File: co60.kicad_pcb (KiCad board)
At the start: 2 copper layers, 285 x 95.1 mm, 251 parts, among them J1 Conn_01x06, Q1 FMMT493TA, SW1 SW_Push, U1 ATMEGA32U4, Y1 16MHz

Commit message: Update: Clean up routing and add some header labels
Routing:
- net LEDPWM: track 25.7 -> 22.6 mm
- net ROW2: track 324.2 -> 322.6 mm
- net LEDGND: track 1543.0 -> 1541.9 mm
- net ROW1: track 329.4 -> 328.6 mm
- net COL11: track 292.1 -> 291.4 mm
- net COL10: track 262.8 -> 262.1 mm
- net COL13: track 348.2 -> 348.9 mm
- net COL3: track 107.2 -> 107.9 mm
- net COL12: track 292.9 -> 293.6 mm
- net Net-(K_LGUI1-Pad4): track 12.3 -> 11.7 mm
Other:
- board text added: "GND"
- board text added: "MISO"
- board text added: "MOSI"
- board text added: "RST"
- board text added: "SCLK"
- board text added: "VCC"

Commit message: Update: A couple of routes
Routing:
- net Net-(D25-Pad2): track 6.72 -> 7.26 mm
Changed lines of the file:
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@@
     (thickness 1.6)
     (drawings 6)
-    (tracks 2795)
+    (tracks 2799)
     (zones 0)
     (modules 251)
@@
   (segment (start 256.83025 75.8825) (end 258.365625 77.417875) (width 0.254) (layer B.Cu) (net 31))
   (segment (start 258.365625 77.417875) (end 258.365625 78.121875) (width 0.254) (layer B.Cu) (net 31))
-  (segment (start 271.62125 75.8825) (end 273.860625 78.121875) (width 0.254) (layer B.Cu) (net 32))
-  (segment (start 273.860625 78.121875) (end 277.415625 78.121875) (width 0.254) (layer B.Cu) (net 32))
-  (segment (start 290.67125 75.8825) (end 292.910625 78.121875) (width 0.254) (layer B.Cu) (net 33))
-  (segment (start 292.910625 78.121875) (end 296.465625 78.121875) (width 0.254) (layer B.Cu) (net 33))
+  (segment (start 271.62125 75.8825) (end 275.88025 75.8825) (width 0.254) (layer B.Cu) (net 32))
+  (segment (start 275.88025 75.8825) (end 277.415625 77.417875) (width 0.254) (layer B.Cu) (net 32))
+  (segment (start 277.415625 77.417875) (end 277.415625 78.121875) (width 0.254) (layer B.Cu) (net 32))
+  (segment (start 271.62125 75.8825) (end 271.71015 75.9714) (width 0.254) (layer B.Cu) (net 32))
+  (segment (start 290.67125 75.8825) (end 294.93025 75.8825) (width 0.254) (layer B.Cu) (net 33))
+  (segment (start 294.93025 75.8825) (end 296.465625 77.417875) (width 0.254) (layer B.Cu) (net 33))
+  (segment (start 296.465625 77.417875) (end 296.465625 78.121875) (width 0.254) (layer B.Cu) (net 33))
+  (segment (start 290.67125 75.8825) (end 290.70935 75.9206) (width 0.254) (layer B.Cu) (net 33))
   (segment (start 309.72125 75.8825) (end 313.98025 75.8825) (width 0.254) (layer B.Cu) (net 34))
   (segment (start 313.98025 75.8825) (end 315.515625 77.417875) (width 0.254) (layer B.Cu) (net 34))

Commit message: Update: Temporarily increase my net clearance values, and re-routing
I noticed in some other designs that the traces were farther
from drill holes and pads than I was putting mine, so I
figured I'd change that. I'm temporarily increasing
my clearance to 0.35 (from 0.2032) and I'm using the
OpenGL router to move my traces farther from holes and
pads. I'll put my clearance back when I'm done. The next switch
to adjust is K_#8
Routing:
- net ROW0: track 365.3 -> 366.2 mm
- net Net-(K_#7-Pad4): track 4.16 -> 5.07 mm
- net Net-(K_#6-Pad4): track 4.28 -> 5.07 mm
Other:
- net class Default: clearance 0.2032 -> 0.35
- net class Power: clearance 0.2032 -> 0.35
- rule trace_clearance: 0.2032 -> 0.35

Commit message: Update: More routing adjustments to increase clearances
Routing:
- net VCC: track 1753.0 -> 1755.1 mm
- net ROW0: track 366.2 -> 364.7 mm, vias 6 -> 8
- net ROW1: track 328.6 -> 329.1 mm, vias 6 -> 8

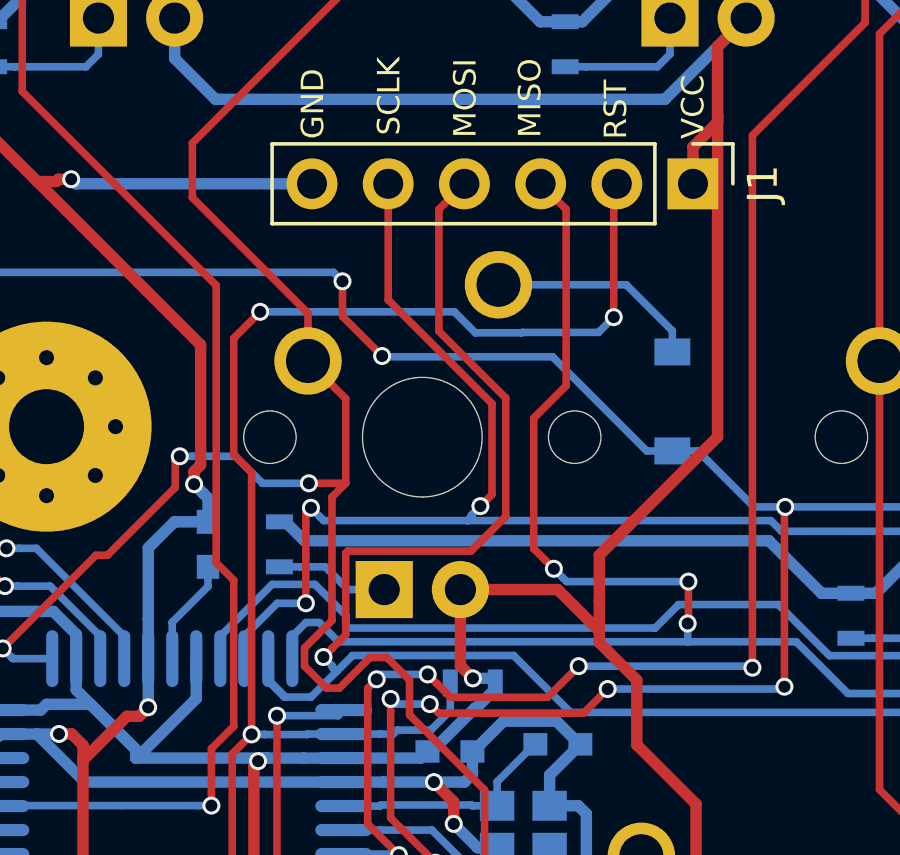
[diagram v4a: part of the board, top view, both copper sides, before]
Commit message: Update: Move more tracks to increase clearance
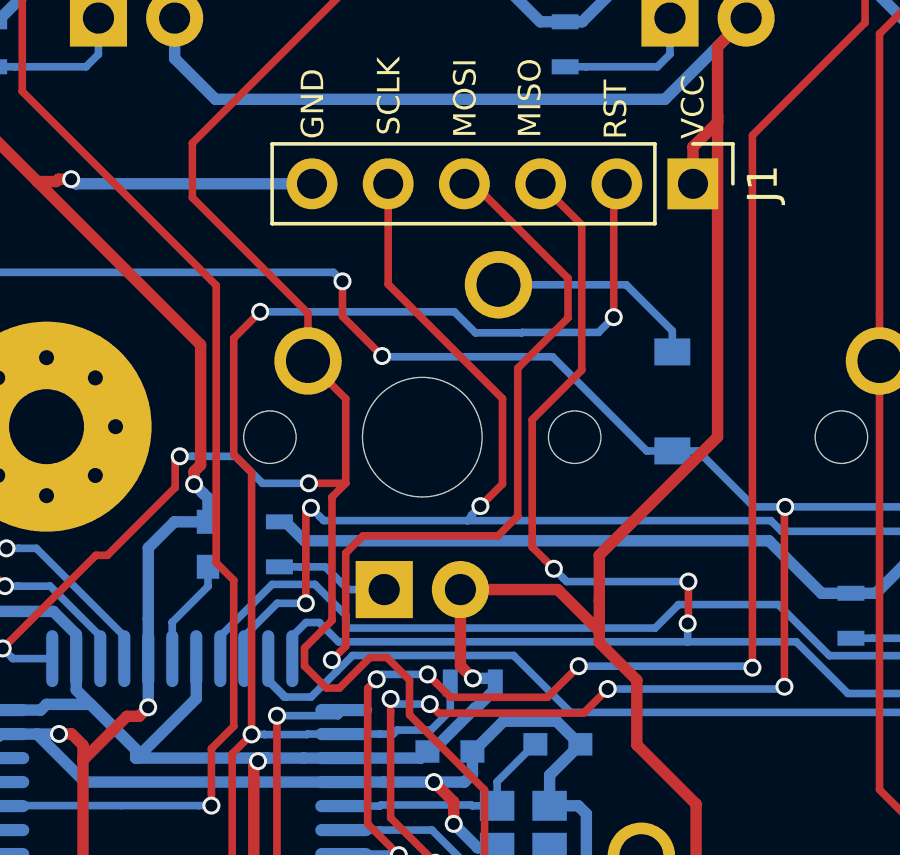
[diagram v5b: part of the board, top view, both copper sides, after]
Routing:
- net COL8: track 249.2 -> 250.4 mm
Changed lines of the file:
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@@
     (thickness 1.6)
     (drawings 6)
-    (tracks 2823)
+    (tracks 2822)
     (zones 0)
     (modules 251)
@@
   (segment (start 108.10875 133.19125) (end 108.10875 116.5225) (width 0.254) (layer F.Cu) (net 82))
   (segment (start 112.87125 135.5725) (end 110.49 135.5725) (width 0.254) (layer F.Cu) (net 82))
-  (segment (start 118.758749 96.347501) (end 117.63375 97.4725) (width 0.254) (layer F.Cu) (net 83))
-  (segment (start 118.758749 92.723749) (end 118.758749 96.347501) (width 0.254) (layer F.Cu) (net 83))
-  (segment (start 113.671338 82.957211) (end 113.671338 87.071962) (width 0.254) (layer F.Cu) (net 83))
-  (segment (start 114.937302 88.30679) (end 115.50309 88.30679) (width 0.254) (layer F.Cu) (net 83))
+  (segment (start 113.671338 87.071962) (end 112.755398 87.987902) (width 0.254) (layer F.Cu) (net 83))
   (segment (start 112.755398 87.987902) (end 112.755398 88.592898) (width 0.254) (layer F.Cu) (net 83))
   (segment (start 116.2558 90.2208) (end 118.758749 92.723749) (width 0.254) (layer F.Cu) (net 83))
-  (segment (start 113.671338 87.071962) (end 112.755398 87.987902) (width 0.254) (layer F.Cu) (net 83))
-  (segment (start 116.2558 89.0595) (end 116.2558 90.2208) (width 0.254) (layer F.Cu) (net 83))
-  (segment (start 115.50309 88.30679) (end 116.2558 89.0595) (width 0.254) (layer F.Cu) (net 83))
+  (segment (start 113.671338 82.957211) (end 113.671338 87.071962) (width 0.254) (layer F.Cu) (net 83))
   (segment (start 113.91709 89.327002) (end 114.937302 88.30679) (width 0.254) (layer F.Cu) (net 83))
+  (segment (start 114.937302 88.30679) (end 115.50309 88.30679) (width 0.254) (layer F.Cu) (net 83))
+  (segment (start 115.50309 88.30679) (end 116.2558 89.0595) (width 0.254) (layer F.Cu) (net 83))
+  (segment (start 116.2558 89.0595) (end 116.2558 90.2208) (width 0.254) (layer F.Cu) (net 83))
+  (segment (start 118.758749 92.723749) (end 118.758749 96.347501) (width 0.254) (layer F.Cu) (net 83))
+  (segment (start 118.758749 96.347501) (end 117.63375 97.4725) (width 0.254) (layer F.Cu) (net 83))
+  (segment (start 114.128549 82.5) (end 113.671338 82.957211) (width 0.254) (layer F.Cu) (net 83))
   (segment (start 112.755398 88.592898) (end 113.489502 89.327002) (width 0.254) (layer F.Cu) (net 83))
   (segment (start 113.489502 89.327002) (end 113.91709 89.327002) (width 0.254) (layer F.Cu) (net 83))
-  (segment (start 114.128549 82.5) (end 113.671338 82.957211) (width 0.254) (layer F.Cu) (net 83))
   (segment (start 122.39625 59.3725) (end 120.80526 59.3725) (width 0.254) (layer F.Cu) (net 83))
   (segment (start 120.80526 59.3725) (end 109.0168 71.16096) (width 0.254) (layer F.Cu) (net 83))
@@
   (segment (start 197.00526 59.3725) (end 189.07125 67.30651) (width 0.254) (layer F.Cu) (net 87))
   (segment (start 189.07125 67.30651) (end 189.07125 76.83151) (width 0.254) (layer F.Cu) (net 87))
+  (segment (start 115.5446 72.517) (end 115.5446 75.8698) (width 0.254) (layer F.Cu) (net 88))
+  (segment (start 119.3546 82.5246) (end 118.618 83.2612) (width 0.254) (layer F.Cu) (net 88))
+  (segment (start 115.5446 75.8698) (end 119.3546 79.6798) (width 0.254) (layer F.Cu) (net 88))
+  (segment (start 119.3546 79.6798) (end 119.3546 82.5246) (width 0.254) (layer F.Cu) (net 88))
   (segment (start 118.318001 83.561199) (end 118.318001 83.612011) (width 0.254) (layer B.Cu) (net 88))
-  (segment (start 119.005351 82.873849) (end 118.618 83.2612) (width 0.254) (layer F.Cu) (net 88))
   (via (at 118.618 83.2612) (size 0.6) (drill 0.4) (layers F.Cu B.Cu) (net 88))
-  (segment (start 115.5446 76.38618) (end 119.005351 79.846931) (width 0.254) (layer F.Cu) (net 88))
-  (segment (start 119.005351 79.846931) (end 119.005351 82.873849) (width 0.254) (layer F.Cu) (net 88))
-  (segment (start 115.5446 72.517) (end 115.5446 76.38618) (width 0.254) (layer F.Cu) (net 88))
   (segment (start 118.318001 83.612011) (end 118.1862 83.743812) (width 0.254) (layer B.Cu) (net 88))
   (segment (start 118.618 83.2612) (end 118.318001 83.561199) (width 0.254) (layer B.Cu) (net 88))
@@
   (segment (start 212.88375 106.9975) (end 222.40875 116.5225) (width 0.254) (layer F.Cu) (net 88))
   (segment (start 208.12125 92.71) (end 212.88375 97.4725) (width 0.254) (layer F.Cu) (net 88))
-  (segment (start 118.0846 72.517) (end 117.234601 73.366999) (width 0.254) (layer F.Cu) (net 89))
-  (via (at 113.3856 88.2904) (size 0.6) (drill 0.4) (layers F.Cu B.Cu) (net 89))
-  (segment (start 113.685599 88.590399) (end 113.685599 88.634099) (width 0.254) (layer B.Cu) (net 89))
-  (segment (start 113.685599 88.634099) (end 113.8245 88.773) (width 0.254) (layer B.Cu) (net 89))
-  (segment (start 113.3856 88.2904) (end 113.685599 88.590399) (width 0.254) (layer B.Cu) (net 89))
-  (segment (start 113.685599 87.990401) (end 113.3856 88.2904) (width 0.254) (layer F.Cu) (net 89))
-  (segment (start 118.306101 84.759799) (end 114.194589 84.759799) (width 0.254) (layer F.Cu) (net 89))
-  (segment (start 117.234601 73.366999) (end 117.234601 77.429588) (width 0.254) (layer F.Cu) (net 89))
-  (segment (start 119.462562 79.657549) (end 119.462562 83.603338) (width 0.254) (layer F.Cu) (net 89))
-  (segment (start 119.462562 83.603338) (end 118.306101 84.759799) (width 0.254) (layer F.Cu) (net 89))
-  (segment (start 117.234601 77.429588) (end 119.462562 79.657549) (width 0.254) (layer F.Cu) (net 89))
-  (segment (start 114.194589 84.759799) (end 114.128549 84.825839) (width 0.254) (layer F.Cu) (net 89))
-  (segment (start 114.128549 87.547451) (end 113.685599 87.990401) (width 0.254) (layer F.Cu) (net 89))
-  (segment (start 114.128549 84.825839) (end 114.128549 87.547451) (width 0.254) (layer F.Cu) (net 89))
+  (segment (start 113.665 88.392) (end 114.128549 87.928451) (width 0.254) (layer F.Cu) (net 89))
+  (segment (start 114.128549 87.928451) (end 114.128549 84.825839) (width 0.254) (layer F.Cu) (net 89))
+  (segment (start 114.128549 84.825839) (end 114.702588 84.2518) (width 0.254) (layer F.Cu) (net 89))
+  (segment (start 119.2022 84.2518) (end 119.8626 83.5914) (width 0.254) (layer F.Cu) (net 89))
+  (segment (start 119.8626 83.5914) (end 119.8626 78.6638) (width 0.254) (layer F.Cu) (net 89))
+  (segment (start 118.3894 72.517) (end 118.0846 72.517) (width 0.254) (layer F.Cu) (net 89))
+  (segment (start 114.702588 84.2518) (end 119.2022 84.2518) (width 0.254) (layer F.Cu) (net 89))
+  (segment (start 121.539 75.6666) (end 118.3894 72.517) (width 0.254) (layer F.Cu) (net 89))
+  (segment (start 119.8626 78.6638) (end 121.539 76.9874) (width 0.254) (layer F.Cu) (net 89))
+  (segment (start 121.539 76.9874) (end 121.539 75.6666) (width 0.254) (layer F.Cu) (net 89))
+  (segment (start 113.8245 88.773) (end 113.8245 88.5515) (width 0.254) (layer B.Cu) (net 89))
+  (via (at 113.665 88.392) (size 0.6) (drill 0.4) (layers F.Cu B.Cu) (net 89))
+  (segment (start 113.8245 88.5515) (end 113.665 88.392) (width 0.254) (layer B.Cu) (net 89))
   (segment (start 225.190063 90.136448) (end 224.765799 90.136448) (width 0.254) (layer F.Cu) (net 89))
   (segment (start 227.17125 89.9) (end 226.934802 90.136448) (width 0.254) (layer F.Cu) (net 89))
@@
   (segment (start 89.05875 78.4225) (end 89.05875 95.09125) (width 0.254) (layer F.Cu) (net 94))
   (segment (start 89.05875 95.09125) (end 86.6775 97.4725) (width 0.254) (layer F.Cu) (net 94))
-  (segment (start 120.6246 72.517) (end 121.474599 73.366999) (width 0.254) (layer F.Cu) (net 95))
-  (segment (start 121.474599 73.366999) (end 121.474599 79.248189) (width 0.254) (layer F.Cu) (net 95))
-  (segment (start 121.474599 79.248189) (end 120.396 80.326788) (width 0.254) (layer F.Cu) (net 95))
-  (segment (start 120.396 80.326788) (end 120.396 84.67799) (width 0.254) (layer F.Cu) (net 95))
-  (segment (start 120.396 84.67799) (end 120.766801 85.048791) (width 0.254) (layer F.Cu) (net 95))
+  (segment (start 120.6246 72.517) (end 121.996211 73.888611) (width 0.254) (layer F.Cu) (net 95))
+  (segment (start 121.996211 73.888611) (end 121.996211 78.726577) (width 0.254) (layer F.Cu) (net 95))
+  (segment (start 121.996211 78.726577) (end 120.3452 80.377588) (width 0.254) (layer F.Cu) (net 95))
+  (segment (start 120.3452 80.377588) (end 120.3452 84.62719) (width 0.254) (layer F.Cu) (net 95))
+  (segment (start 120.3452 84.62719) (end 120.766801 85.048791) (width 0.254) (layer F.Cu) (net 95))
   (segment (start 120.766801 85.048791) (end 121.0668 85.34879) (width 0.254) (layer F.Cu) (net 95))
   (segment (start 331.94625 59.3725) (end 330.6445 59.3725) (width 0.254) (layer F.Cu) (net 95))

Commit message: Update: More work on increasing clearances
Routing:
- net VCC: track 1755.1 -> 1797.7 mm
- net COL14: track 378.9 -> 392.3 mm
- net LEDGND: track 1542.4 -> 1550.9 mm, vias 22 -> 20
- net ROW3: track 330.1 -> 334.0 mm
- net ROW1: track 329.1 -> 332.6 mm
- net ROW4: track 349.0 -> 351.8 mm
- net ROW2: track 322.6 -> 325.1 mm
- net COL0: track 111.2 -> 113.8 mm
- net COL12: track 293.6 -> 295.3 mm
- net COL1: track 94.6 -> 95.6 mm
- net COL6: track 197.0 -> 197.8 mm
- net Net-(K_SPACE2_1-Pad4): track 29.5 -> 28.8 mm
- net COL8: track 250.4 -> 249.9 mm
- net Net-(K_ENTER1-Pad4): track 23.2 -> 23.7 mm
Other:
- net class Default: clearance 0.35 -> 0.2032
- net class Power: clearance 0.35 -> 0.2032
- rule trace_clearance: 0.35 -> 0.2032

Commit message: Update: Run cleanup pads and traces
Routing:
- net VCC: track 1797.7 -> 1788.2 mm

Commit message: Update: Move some more traces, and some component text on silk screen
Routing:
- net ROW4: track 351.8 -> 356.9 mm
- net VCC: track 1788.2 -> 1789.8 mm
- net ROW2: track 325.1 -> 326.0 mm
- net LEDGND: track 1550.9 -> 1551.7 mm
- net Net-(C1-Pad1): track 10.6 -> 9.86 mm
